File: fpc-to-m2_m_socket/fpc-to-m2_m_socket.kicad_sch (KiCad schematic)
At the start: 22 parts, among them J2 Bus_M.2_Socket_M, J5 Conn_01x02_Pin, Y1 OK2EL89CJI-111YLC-32.768K

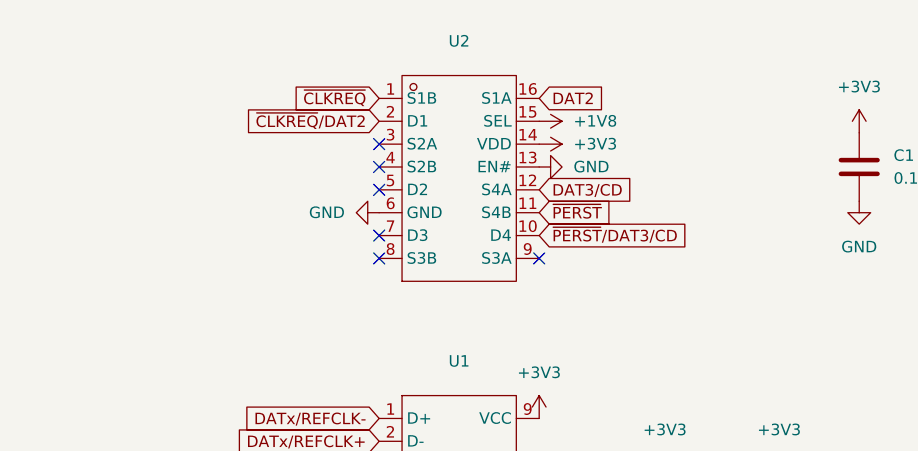
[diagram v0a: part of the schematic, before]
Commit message: fpc-to-m2_m_socket: switch TMUX1574 to TSSOP-16
The UQFN-16 variant just went out of stock at jlcpcb.
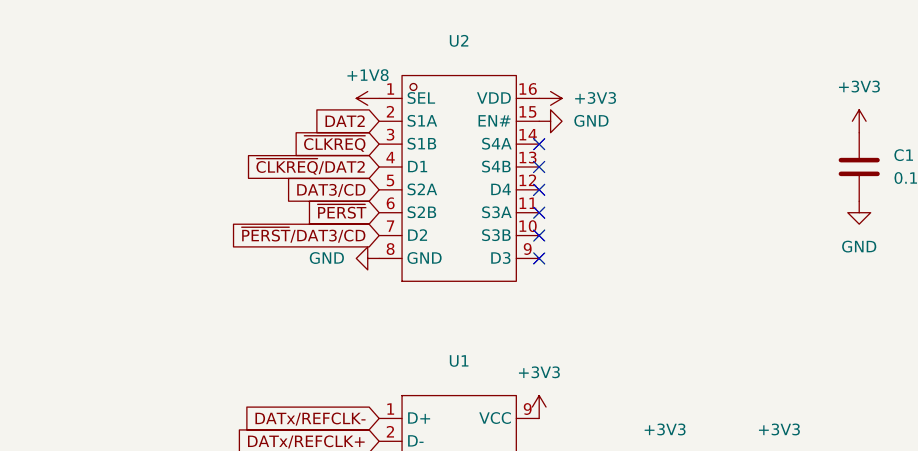
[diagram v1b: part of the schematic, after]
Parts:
- U2: footprint m1cha:tmux1574 -> Package_SO:TSSOP-16_4.4x5mm_P0.65mm; symbol m1cha:TMUX1574RSVR-UQFN -> m1cha:TMUX1574PWR; LCSC Part # C2673120 -> C2673443; Manufacturer Part TMUX1574RSVR -> TMUX1574PWR
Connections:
- net +1V8: now also U2.1 (SEL); no longer U2.15 (SEL)
- net +3V3: now also U2.16 (VDD); no longer U2.14 (VDD)
- net DAT2: now also U2.2 (S1A); no longer U2.16 (S1A)
- net DAT3/CD: now also U2.5 (S2A); no longer U2.12 (S4A)
- net GND: now also U2.15 (EN#), U2.8 (GND); no longer U2.13 (EN#), U2.6 (GND)
- net ~{CLKREQ}: now also U2.3 (S1B); no longer U2.1 (S1B)
- net ~{CLKREQ}/DAT2: now also U2.4 (D1); no longer U2.2 (D1)
- net ~{PERST}: now also U2.6 (S2B); no longer U2.11 (S4B)
- net ~{PERST}/DAT3/CD: now also U2.7 (D2); no longer U2.10 (D4)
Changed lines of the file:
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@@
 	)
 	(no_connect
-		(at 127 27.94)
+		(at 144.78 30.48)
 	)
 	(no_connect
-		(at 127 38.1)
+		(at 144.78 40.64)
 	)
 	(no_connect
@@
 	)
 	(no_connect
-		(at 144.78 40.64)
+		(at 144.78 27.94)
 	)
 	(no_connect
@@
 	)
 	(no_connect
-		(at 127 30.48)
+		(at 144.78 33.02)
 	)
 	(no_connect
@@
 	)
 	(no_connect
-		(at 127 33.02)
+		(at 144.78 35.56)
 	)
 	(no_connect
@@
 	)
 	(no_connect
-		(at 127 40.64)
+		(at 144.78 38.1)
 	)
 	(no_connect
@@
 	(global_label "~{CLKREQ}"
 		(shape input)
-		(at 127 22.86 180)
+		(at 127 27.94 180)
 		(fields_autoplaced yes)
 		(effects
@@
 		)
 		(property "Intersheetrefs" "${INTERSHEET_REFS}"
-			(at 116.6972 22.86 0)
+			(at 116.6972 27.94 0)
 			(effects
 				(font
@@
 	(global_label "DAT2"
 		(shape input)
-		(at 144.78 22.86 0)
+		(at 127 25.4 180)
 		(fields_autoplaced yes)
 		(effects
@@
 				(size 1.27 1.27)
 			)
-			(justify left)
+			(justify right)
 		)
 		(property "Intersheetrefs" "${INTERSHEET_REFS}"
-			(at 152.3009 22.86 0)
+			(at 119.4791 25.4 0)
 			(effects
 				(font
 					(size 1.27 1.27)
 				)
-				(justify left)
+				(justify right)
 				(hide yes)
 			)
@@
 	(global_label "~{CLKREQ}{slash}DAT2"
 		(shape input)
-		(at 127 25.4 180)
+		(at 127 30.48 180)
 		(fields_autoplaced yes)
 		(effects
@@
 		)
 		(property "Intersheetrefs" "${INTERSHEET_REFS}"
-			(at 110.831 25.4 0)
+			(at 110.831 30.48 0)
 			(effects
 				(font
@@
 	(global_label "DAT3{slash}CD"
 		(shape input)
-		(at 144.78 33.02 0)
+		(at 127 33.02 180)
 		(fields_autoplaced yes)
 		(effects
@@
 				(size 1.27 1.27)
 			)
-			(justify left)
+			(justify right)
 		)
 		(property "Intersheetrefs" "${INTERSHEET_REFS}"
-			(at 156.1714 33.02 0)
+			(at 115.6086 33.02 0)
 			(effects
 				(font
 					(size 1.27 1.27)
 				)
-				(justify left)
+				(justify right)
 				(hide yes)
 			)
@@
 	(global_label "~{PERST}{slash}DAT3{slash}CD"
 		(shape input)
-		(at 144.78 38.1 0)
+		(at 127 38.1 180)
 		(fields_autoplaced yes)
 		(effects
@@
 				(size 1.27 1.27)
 			)
-			(justify left)
+			(justify right)
 		)
 		(property "Intersheetrefs" "${INTERSHEET_REFS}"
-			(at 163.368 38.1 0)
+			(at 108.412 38.1 0)
 			(effects
 				(font
 					(size 1.27 1.27)
 				)
-				(justify left)
+				(justify right)
 				(hide yes)
 			)
@@
 	(global_label "~{PERST}"
 		(shape input)
-		(at 144.78 35.56 0)
+		(at 127 35.56 180)
 		(fields_autoplaced yes)
 		(effects
@@
 				(size 1.27 1.27)
 			)
-			(justify left)
+			(justify right)
 		)
 		(property "Intersheetrefs" "${INTERSHEET_REFS}"
-			(at 153.6313 35.56 0)
+			(at 118.1487 35.56 0)
 			(effects
 				(font
 					(size 1.27 1.27)
 				)
-				(justify left)
+				(justify right)
 				(hide yes)
 			)
@@
 	(symbol
 		(lib_id "power:GND")
-		(at 144.78 30.48 90)
+		(at 144.78 25.4 90)
 		(unit 1)
 		(exclude_from_sim no)
@@
 		(fields_autoplaced yes)
 		(property "Reference" "#PWR015"
-			(at 151.13 30.48 0)
+			(at 151.13 25.4 0)
 			(effects
 				(font
@@
 		)
 		(property "Value" "GND"
-			(at 148.59 30.4799 90)
+			(at 148.59 25.3999 90)
 			(effects
 				(font
@@
 		)
 		(property "Footprint" ""
-			(at 144.78 30.48 0)
+			(at 144.78 25.4 0)
 			(effects
 				(font
@@
 		)
 		(property "Datasheet" ""
-			(at 144.78 30.48 0)
+			(at 144.78 25.4 0)
 			(effects
 				(font
@@
 		)
 		(property "Description" "Power symbol creates a global label with name \"GND\" , ground"
-			(at 144.78 30.48 0)
+			(at 144.78 25.4 0)
 			(effects
 				(font
@@
 	(symbol
 		(lib_id "power:GND")
-		(at 127 35.56 270)
+		(at 127 40.64 270)
 		(unit 1)
 		(exclude_from_sim no)
@@
 		(fields_autoplaced yes)
 		(property "Reference" "#PWR014"
-			(at 120.65 35.56 0)
+			(at 120.65 40.64 0)
 			(effects
 				(font
@@
 		)
 		(property "Value" "GND"
-			(at 123.19 35.5599 90)
+			(at 123.19 40.6399 90)
 			(effects
 				(font
@@
 		)
 		(property "Footprint" ""
-			(at 127 35.56 0)
+			(at 127 40.64 0)
 			(effects
 				(font
@@
 		)
 		(property "Datasheet" ""
-			(at 127 35.56 0)
+			(at 127 40.64 0)
 			(effects
 				(font
@@
 		)
 		(property "Description" "Power symbol creates a global label with name \"GND\" , ground"
-			(at 127 35.56 0)
+			(at 127 40.64 0)
 			(effects
 				(font
@@
 	(symbol
 		(lib_id "power:+3V3")
-		(at 144.78 27.94 270)
+		(at 144.78 22.86 270)
 		(unit 1)
 		(exclude_from_sim no)
@@
 		(fields_autoplaced yes)
 		(property "Reference" "#PWR050"
-			(at 140.97 27.94 0)
+			(at 140.97 22.86 0)
 			(effects
 				(font
@@
 		)
 		(property "Value" "+3V3"
-			(at 148.59 27.9399 90)
+			(at 148.59 22.8599 90)
 			(effects
 				(font
@@
 		)
 		(property "Footprint" ""
-			(at 144.78 27.94 0)
+			(at 144.78 22.86 0)
 			(effects
 				(font
@@
 		)
 		(property "Datasheet" ""
-			(at 144.78 27.94 0)
+			(at 144.78 22.86 0)
 			(effects
 				(font
@@
 		)
 		(property "Description" "Power symbol creates a global label with name \"+3V3\""
-			(at 144.78 27.94 0)
+			(at 144.78 22.86 0)
 			(effects
 				(font
@@
 	)
 	(symbol
-		(lib_id "m1cha:TMUX1574RSVR-UQFN")
+		(lib_id "m1cha:TMUX1574PWR")
 		(at 135.89 31.75 0)
 		(unit 1)
@@
 			)
 		)
-		(property "Footprint" "m1cha:tmux1574"
+		(property "Footprint" "Package_SO:TSSOP-16_4.4x5mm_P0.65mm"
 			(at 135.89 31.75 0)
 			(effects
@@
 			)
 		)
-		(property "Datasheet" "https://www.ti.com/lit/ds/symlink/tmux1574.pdf"
+		(property "Datasheet" "https://www.ti.com/cn/lit/gpn/tmux1574"
 			(at 135.89 31.75 0)
 			(effects
@@
 			)
 		)
-		(property "Description" "Switch Circuit:SPDT(SPDT) Number of Channels:4 Supply Voltage:1.5V~5.5V Supply Voltage:1.5V~5.5V Turn-on time:35us On-State Resistance (Max):4.5Ω Turn-off time:95ns Operating Temperature:-40°C~+125°C Operating Temperature:-40°C~+125°C"
+		(property "Description" "Switch Circuit:SPDT(SPDT) Number of Channels:4 Supply Voltage:1.5V~5.5V Supply Voltage:1.5V~5.5V Turn-on time:35ns On-State Resistance (Max):4.5Ω Turn-off time:6ns Operating Temperature:-40°C~+125°C Operating Temperature:-40°C~+125°C"
 			(at 135.89 31.75 0)
 			(effects
@@
 			)
 		)
-		(property "Manufacturer Part" "TMUX1574RSVR"
+		(property "Manufacturer Part" "TMUX1574PWR"
 			(at 135.89 31.75 0)
 			(effects
@@
 			)
 		)
-		(property "LCSC Part #" "C2673120"
+		(property "LCSC Part #" "C2673443"
 			(at 135.89 31.75 0)
 			(effects
@@
 	(symbol
 		(lib_id "power:+1V8")
-		(at 144.78 25.4 270)
+		(at 127 22.86 90)
 		(unit 1)
 		(exclude_from_sim no)
@@
 		(fields_autoplaced yes)
 		(property "Reference" "#PWR017"
-			(at 140.97 25.4 0)
+			(at 130.81 22.86 0)
 			(effects
 				(font
@@
 		)
 		(property "Value" "+1V8"
-			(at 148.59 25.3999 90)
+			(at 125.73 20.32 90)
 			(effects
 				(font
 					(size 1.27 1.27)
 				)
-				(justify left)
 			)
 		)
 		(property "Footprint" ""
-			(at 144.78 25.4 0)
+			(at 127 22.86 0)
 			(effects
 				(font
@@
 		)
 		(property "Datasheet" ""
-			(at 144.78 25.4 0)
+			(at 127 22.86 0)
 			(effects
 				(font
@@
 		)
 		(property "Description" "Power symbol creates a global label with name \"+1V8\""
-			(at 144.78 25.4 0)
+			(at 127 22.86 0)
 			(effects
 				(font
